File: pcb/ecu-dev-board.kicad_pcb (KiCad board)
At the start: 4 copper layers, 99.9 x 99.9 mm, 218 parts, among them IC1 MAX9924UAUB+, IC2 74HC14D-Q100,118, IC3 UCC28910DR, IC4 UCC27624QDRQ1, J1 MX23A18NF1, J2 39-30-1020, K1 Relay, Q1 MMBT2222A, Q10 AO3400A, Q2 IRLIZ44N, Q3 HL2303, Q4 STGB20M65DF2, Q5 MMBT2222A, Q6 MMBT2222A, Q7 MMBT2222A, Q8 MMBTA55, Q9 MMBTA55, T1 SM-LP-5001E, U1 WeMos_S2_mini, U2 OPA2376xxD, U3 TPS54202DDC, U4 AT223-CuH-S

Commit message: organized pcb
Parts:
- moved JP10 142.6 mm to (134.5, 188.7)
- moved TP24 135.6 mm to (39.1, 151.6)
- moved TP25 135.6 mm to (39.1, 154.7)
- moved TP26 135.6 mm to (39.1, 157.7)
- moved JP4 131.7 mm to (139.3, 185.5)
- moved JP7 131.7 mm to (139.3, 192.6)
- moved JP5 131.7 mm to (139.3, 189.0)
- moved TP30 120.9 mm to (43.8, 152.1)
- moved TP31 120.9 mm to (43.7, 159.6)
- moved TP10 111.3 mm to (34.9, 154.4)
- moved TP11 111.3 mm to (34.9, 157.4)
- moved TP19 111.3 mm to (34.9, 160.5)
- moved TP9 111.3 mm to (34.9, 151.3)
- moved JP8 98.2 mm to (134.4, 178.5)
- moved JP25 98.2 mm to (134.4, 185.6)
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
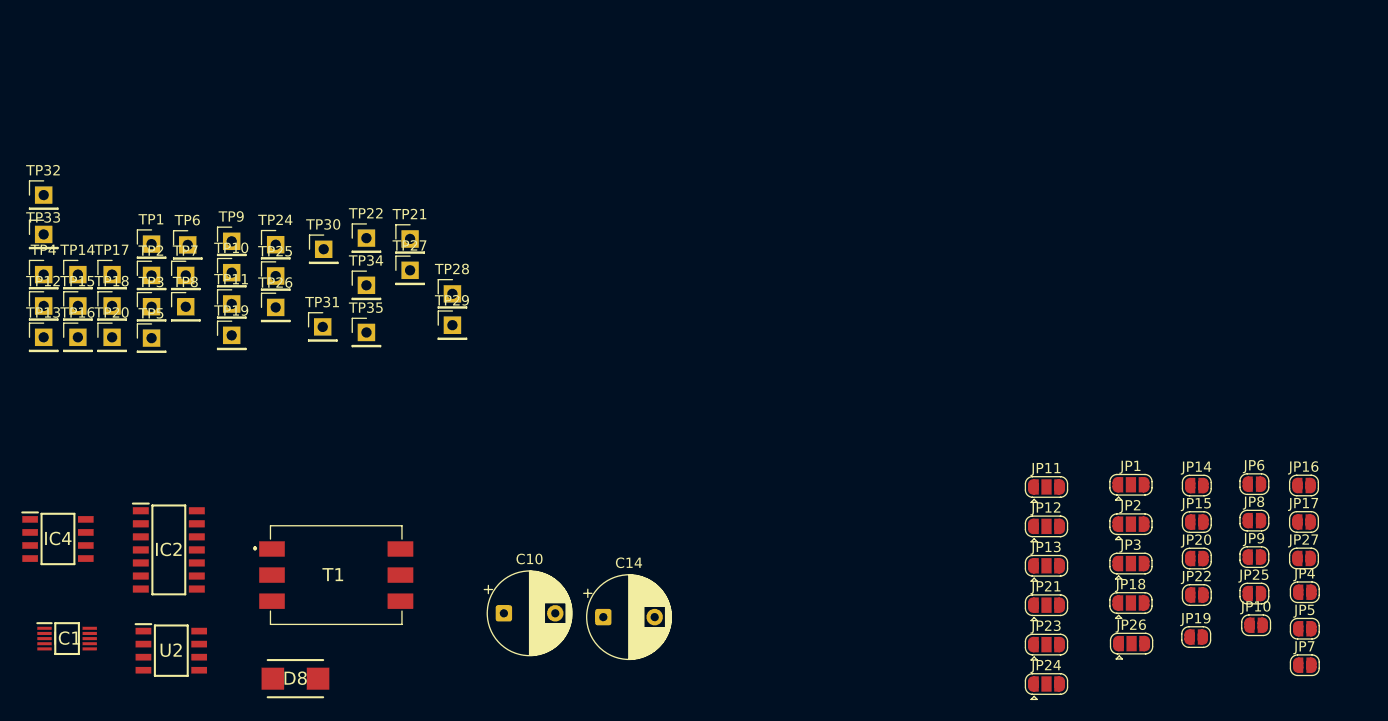
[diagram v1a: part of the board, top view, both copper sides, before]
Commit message: ordered jumpers and test pins
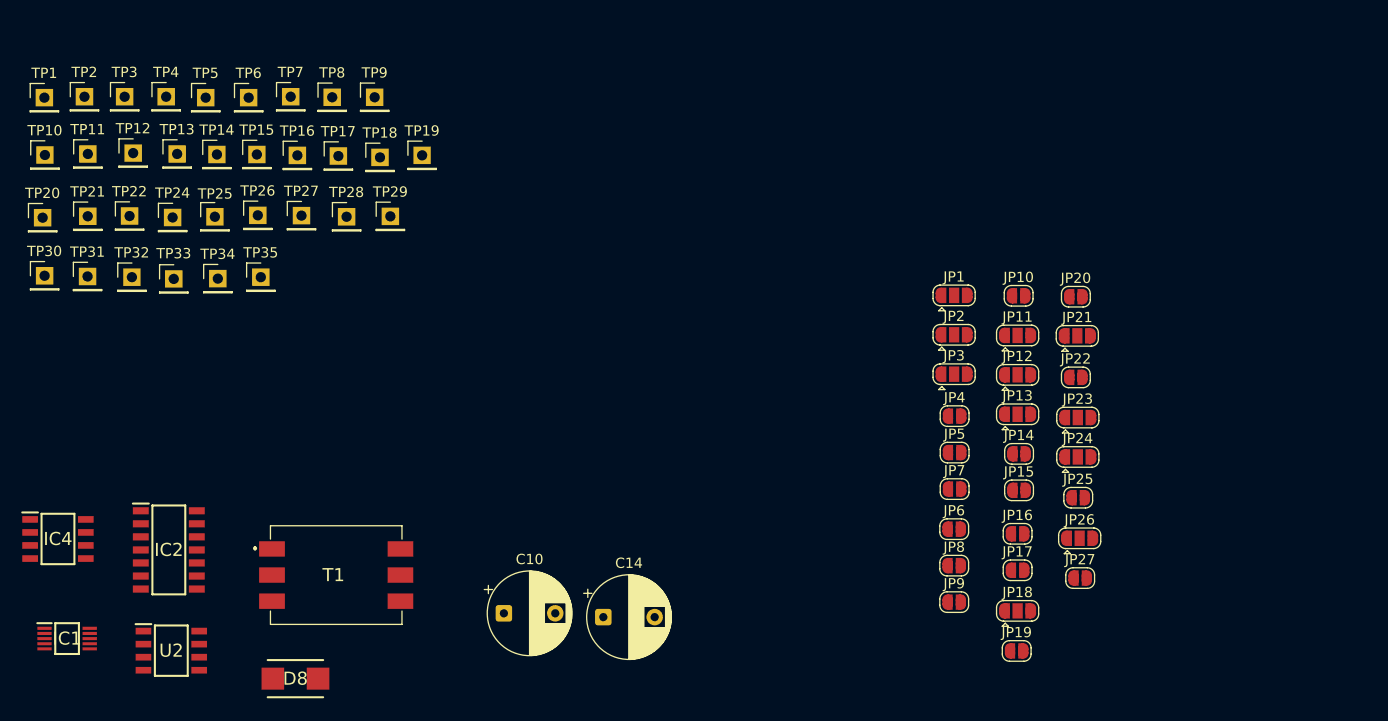
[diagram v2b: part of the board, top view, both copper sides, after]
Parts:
- moved JP10 39.5 mm to (111.4, 156.6)
- moved JP4 38.1 mm to (105.2, 168.3)
- moved JP7 38.1 mm to (105.2, 175.4)
- moved JP5 38.1 mm to (105.2, 171.9)
- moved TP21 31.4 mm to (20.8, 148.9)
- moved TP18 29.8 mm to (49.3, 143.1)
- moved JP6 29.5 mm to (105.2, 179.3)
- moved JP8 29.5 mm to (105.2, 182.9)
- moved JP9 29.5 mm to (105.2, 186.4)
- moved JP16 28.3 mm to (111.3, 179.8)
- moved JP17 28.3 mm to (111.3, 183.3)
- moved JP20 28.1 mm to (117.0, 156.7)
- moved TP16 27.7 mm to (41.2, 142.9)
- moved TP30 27.3 mm to (16.6, 154.7)
- moved JP21 26.4 mm to (117.1, 160.5)
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
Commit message: revision 2.0: added LC Vbatt filtering and changed Pmos protection to be a schttoky
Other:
- board text added: "1 Layer: piste corte (alimentazione solo piste cortissime con via dal layer 4) 2 Layer: tutta massa ininterrotta 3 Layer: segnali 4 Layer: alimentazione"
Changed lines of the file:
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@@
 		(layer "Edge.Cuts")
+	)
+	(gr_text "1 Layer: piste corte (alimentazione solo piste cortissime con via dal layer 4)\n2 Layer: tutta massa ininterrotta\n3 Layer: segnali\n4 Layer: alimentazione"
+		(at 197.92 9.56 0)
+		(layer "Cmts.User")
+		(effects
+			(font
+				(size 1.5 1.5)
+				(thickness 0.3)
+				(bold yes)
+			)
+			(justify left bottom)
+		)
 	)
 	(gr_text "TROPPO GRANDI"

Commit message: revision 2.0: other minor changed
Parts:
- removed BR2: MB10S, SamacSys_Parts:SOP245P670X290-4N
- removed C20: 10u, Capacitor_SMD:C_0603_1608Metric
- removed FB1, FB2: BLM18PG121SN1D, SamacSys_Parts:BLM18SP221SN1B
- removed JP20, JP6: SolderJumper_2_Open, Jumper:SolderJumper-2_P1.3mm_Open_RoundedPad1.0x1.5mm
- removed Q3: HL2303, Package_TO_SOT_SMD:SOT-23
- removed R16: 510k, Resistor_SMD:R_0603_1608Metric
- removed R17: 100k, Resistor_SMD:R_0603_1608Metric
- removed R36: 5k1, Resistor_SMD:R_0603_1608Metric
- added C603: 22u, Capacitor_SMD:C_0805_2012Metric, F.Cu at (110.8, 123.0)
- added C612: 1000u, Capacitor_THT:CP_Radial_D8.0mm_P5.00mm, F.Cu at (66.1, 91.4)
- added C613: 10u, Capacitor_SMD:C_0805_2012Metric, F.Cu at (110.8, 126.1)
- added C614: 1u, Capacitor_SMD:C_0805_2012Metric, F.Cu at (110.8, 129.1)
- added C615: 100n, Capacitor_SMD:C_0805_2012Metric, F.Cu at (110.8, 132.1)
- added D609: SS54, Diode_SMD:D_SMA, F.Cu at (117.1, 123.8)
- added FB601: BLM18PG121SN1D, Inductor_SMD:L_0603_1608Metric, F.Cu at (115.0, 127.3)
- added H601: MountingHole_Pad, MountingHole:MountingHole_3.2mm_M3_DIN965_Pad, F.Cu at (105.0, 113.2)
- added H602: MountingHole_Pad, MountingHole:MountingHole_3.2mm_M3_DIN965_Pad, F.Cu at (105.0, 120.3)
- added H603: MountingHole_Pad, MountingHole:MountingHole_3.2mm_M3_DIN965_Pad, F.Cu at (105.0, 127.5)
- added H604: MountingHole_Pad, MountingHole:MountingHole_3.2mm_M3_DIN965_Pad, F.Cu at (248.9, 116.8)
- added L603: 15u, Inductor_SMD:L_10.4x10.4_H4.8, F.Cu at (114.9, 115.6)
- C201: renamed from C5; footprint Capacitor_SMD:C_0603_1608Metric -> Capacitor_SMD:C_0805_2012Metric
- C202: renamed from C6; footprint Capacitor_SMD:C_0603_1608Metric -> Capacitor_SMD:C_0805_2012Metric
- C203: renamed from C1; footprint Capacitor_SMD:C_0603_1608Metric -> Capacitor_SMD:C_0805_2012Metric
- C204: renamed from C29; footprint Capacitor_SMD:C_0603_1608Metric -> Capacitor_SMD:C_0805_2012Metric
- C205: renamed from C28; footprint Capacitor_SMD:C_0603_1608Metric -> Capacitor_SMD:C_0805_2012Metric
- C206: renamed from C7; footprint Capacitor_SMD:C_0603_1608Metric -> Capacitor_SMD:C_0805_2012Metric
- C207: renamed from C8; footprint Capacitor_SMD:C_0603_1608Metric -> Capacitor_SMD:C_0805_2012Metric
- C208: renamed from C2; footprint Capacitor_SMD:C_0603_1608Metric -> Capacitor_SMD:C_0805_2012Metric
- C209: renamed from C3; footprint Capacitor_SMD:C_0603_1608Metric -> Capacitor_SMD:C_0805_2012Metric
- C210: renamed from C4; footprint Capacitor_SMD:C_0603_1608Metric -> Capacitor_SMD:C_0805_2012Metric
- C401: renamed from C15; footprint Capacitor_SMD:C_0603_1608Metric -> Capacitor_SMD:C_0805_2012Metric
- C402: renamed from C35; footprint Capacitor_SMD:C_0603_1608Metric -> Capacitor_SMD:C_0805_2012Metric
- C403: renamed from C18; footprint Capacitor_SMD:C_0603_1608Metric -> Capacitor_SMD:C_0805_2012Metric
- C404: renamed from C16; footprint Capacitor_SMD:C_0603_1608Metric -> Capacitor_SMD:C_0805_2012Metric
- C405: renamed from C32; footprint Capacitor_SMD:C_0603_1608Metric -> Capacitor_SMD:C_0805_2012Metric
- C406: renamed from C33; footprint Capacitor_SMD:C_0603_1608Metric -> Capacitor_SMD:C_0805_2012Metric
- C407: renamed from C34; footprint Capacitor_SMD:C_0603_1608Metric -> Capacitor_SMD:C_0805_2012Metric
- C408: renamed from C27; footprint Capacitor_SMD:C_0603_1608Metric -> Capacitor_SMD:C_0805_2012Metric
- C409: renamed from C11; footprint Capacitor_SMD:C_0603_1608Metric -> Capacitor_SMD:C_0805_2012Metric
- C410: renamed from C30; footprint Capacitor_SMD:C_0603_1608Metric -> Capacitor_SMD:C_0805_2012Metric
- C411: renamed from C31; footprint Capacitor_SMD:C_0603_1608Metric -> Capacitor_SMD:C_0805_2012Metric
- C604: renamed from C21; footprint Capacitor_SMD:C_0603_1608Metric -> Capacitor_SMD:C_0805_2012Metric
- C605: renamed from C22; footprint Capacitor_SMD:C_0603_1608Metric -> Capacitor_SMD:C_0805_2012Metric
- C606: renamed from C23; footprint Capacitor_SMD:C_0603_1608Metric -> Capacitor_SMD:C_0805_2012Metric
- C608: renamed from C24; footprint Capacitor_SMD:C_0603_1608Metric -> Capacitor_SMD:C_0805_2012Metric
- C609: renamed from C17; footprint Capacitor_SMD:C_0603_1608Metric -> Capacitor_SMD:C_0805_2012Metric
- C610: renamed from C25; footprint Capacitor_SMD:C_0603_1608Metric -> Capacitor_SMD:C_0805_2012Metric
- C611: renamed from C13; footprint Capacitor_SMD:C_0603_1608Metric -> Capacitor_SMD:C_0805_2012Metric
- C616: renamed from C19; value 1m -> 1000u
- C701: renamed from C37; footprint Capacitor_SMD:C_0603_1608Metric -> Capacitor_SMD:C_0805_2012Metric
- C702: renamed from C36; footprint Capacitor_SMD:C_0603_1608Metric -> Capacitor_SMD:C_0805_2012Metric
- C703: renamed from C26; footprint Capacitor_SMD:C_0603_1608Metric -> Capacitor_SMD:C_0805_2012Metric
- IC701: renamed from IC4; value UCC27624QDRQ1 -> UCC27624DR
- L601: renamed from L3; footprint Inductor_SMD:L_SXN_SMDRI125 -> Inductor_SMD:L_10.4x10.4_H4.8
- R201: renamed from R6; footprint Resistor_SMD:R_0603_1608Metric -> Resistor_SMD:R_0805_2012Metric
- R202: renamed from R7; footprint Resistor_SMD:R_0603_1608Metric -> Resistor_SMD:R_0805_2012Metric
- R203: renamed from R4; footprint Resistor_SMD:R_0603_1608Metric -> Resistor_SMD:R_0805_2012Metric
- R204: renamed from R5; footprint Resistor_SMD:R_0603_1608Metric -> Resistor_SMD:R_0805_2012Metric
- R205: renamed from R1; footprint Resistor_SMD:R_0603_1608Metric -> Resistor_SMD:R_0805_2012Metric
- R206: renamed from R2; footprint Resistor_SMD:R_0603_1608Metric -> Resistor_SMD:R_0805_2012Metric
- R207: renamed from R55; footprint Resistor_SMD:R_0603_1608Metric -> Resistor_SMD:R_0805_2012Metric
- R208: renamed from R3; footprint Resistor_SMD:R_0603_1608Metric -> Resistor_SMD:R_0805_2012Metric
- R209: renamed from R8; footprint Resistor_SMD:R_0603_1608Metric -> Resistor_SMD:R_0805_2012Metric
- R210: renamed from R10; footprint Resistor_SMD:R_0603_1608Metric -> Resistor_SMD:R_0805_2012Metric
- R211: renamed from R11; footprint Resistor_SMD:R_0603_1608Metric -> Resistor_SMD:R_0805_2012Metric
- R213: renamed from R12; footprint Resistor_SMD:R_0603_1608Metric -> Resistor_SMD:R_0805_2012Metric
- R214: renamed from R57; footprint Resistor_SMD:R_0603_1608Metric -> Resistor_SMD:R_0805_2012Metric
- R301: renamed from R50; footprint Resistor_SMD:R_0603_1608Metric -> Resistor_SMD:R_0805_2012Metric
- R302: renamed from R51; footprint Resistor_SMD:R_0603_1608Metric -> Resistor_SMD:R_0805_2012Metric
- R303: renamed from R52; footprint Resistor_SMD:R_0603_1608Metric -> Resistor_SMD:R_0805_2012Metric
- R401: renamed from R29; footprint Resistor_SMD:R_0603_1608Metric -> Resistor_SMD:R_0805_2012Metric
- R402: renamed from R30; footprint Resistor_SMD:R_0603_1608Metric -> Resistor_SMD:R_0805_2012Metric
- R403: renamed from R62; footprint Resistor_SMD:R_0603_1608Metric -> Resistor_SMD:R_0805_2012Metric
- R404: renamed from R63; footprint Resistor_SMD:R_0603_1608Metric -> Resistor_SMD:R_0805_2012Metric
- R405: renamed from R28; footprint Resistor_SMD:R_0603_1608Metric -> Resistor_SMD:R_0805_2012Metric
- R406: renamed from R25; footprint Resistor_SMD:R_0603_1608Metric -> Resistor_SMD:R_0805_2012Metric
- R407: renamed from R32; footprint Resistor_SMD:R_0603_1608Metric -> Resistor_SMD:R_0805_2012Metric
- R408: renamed from R31; footprint Resistor_SMD:R_0603_1608Metric -> Resistor_SMD:R_0805_2012Metric
- R409: renamed from R64; footprint Resistor_SMD:R_0603_1608Metric -> Resistor_SMD:R_0805_2012Metric
- R410: renamed from R59; footprint Resistor_SMD:R_0603_1608Metric -> Resistor_SMD:R_0805_2012Metric
- R411: renamed from R60; footprint Resistor_SMD:R_0603_1608Metric -> Resistor_SMD:R_0805_2012Metric
- R412: renamed from R61; footprint Resistor_SMD:R_0603_1608Metric -> Resistor_SMD:R_0805_2012Metric
- R413: renamed from R19; footprint Resistor_SMD:R_0603_1608Metric -> Resistor_SMD:R_0805_2012Metric
- R414: renamed from R53; footprint Resistor_SMD:R_0603_1608Metric -> Resistor_SMD:R_0805_2012Metric
- R415: renamed from R54; footprint Resistor_SMD:R_0603_1608Metric -> Resistor_SMD:R_0805_2012Metric
- R416: renamed from R47; footprint Resistor_SMD:R_0603_1608Metric -> Resistor_SMD:R_0805_2012Metric
- R417: renamed from R58; footprint Resistor_SMD:R_0603_1608Metric -> Resistor_SMD:R_0805_2012Metric
- R418: renamed from R20; footprint Resistor_SMD:R_0603_1608Metric -> Resistor_SMD:R_0805_2012Metric
- R419: renamed from R37; footprint Resistor_SMD:R_0603_1608Metric -> Resistor_SMD:R_0805_2012Metric
- R420: renamed from R22; footprint Resistor_SMD:R_0603_1608Metric -> Resistor_SMD:R_0805_2012Metric
- R421: renamed from R21; footprint Resistor_SMD:R_0603_1608Metric -> Resistor_SMD:R_0805_2012Metric
- R501: renamed from R48; footprint Resistor_SMD:R_0603_1608Metric -> Resistor_SMD:R_0805_2012Metric
- R502: renamed from R68; footprint Resistor_SMD:R_0603_1608Metric -> Resistor_SMD:R_0805_2012Metric
- R503: renamed from R49; footprint Resistor_SMD:R_0603_1608Metric -> Resistor_SMD:R_0805_2012Metric
- R504: renamed from R56; footprint Resistor_SMD:R_0603_1608Metric -> Resistor_SMD:R_0805_2012Metric
- R505: renamed from R15; footprint Resistor_SMD:R_0603_1608Metric -> Resistor_SMD:R_0805_2012Metric
- R506: renamed from R45; footprint Resistor_SMD:R_0603_1608Metric -> Resistor_SMD:R_0805_2012Metric
- R507: renamed from R13; footprint Resistor_SMD:R_0603_1608Metric -> Resistor_SMD:R_0805_2012Metric
- R508: renamed from R46; footprint Resistor_SMD:R_0603_1608Metric -> Resistor_SMD:R_0805_2012Metric
- R509: renamed from R67; footprint Resistor_SMD:R_0603_1608Metric -> Resistor_SMD:R_0805_2012Metric
- R510: renamed from R18; value 330k -> 1M; footprint Resistor_SMD:R_0603_1608Metric -> Resistor_SMD:R_0805_2012Metric
- R602: renamed from R34; footprint Resistor_SMD:R_0603_1608Metric -> Resistor_SMD:R_0805_2012Metric
- R603: renamed from R9; footprint Resistor_SMD:R_0603_1608Metric -> Resistor_SMD:R_0805_2012Metric
- R604: renamed from R33; footprint Resistor_SMD:R_0603_1608Metric -> Resistor_SMD:R_0805_2012Metric
- R605: renamed from R24; footprint Resistor_SMD:R_0603_1608Metric -> Resistor_SMD:R_0805_2012Metric
- R606: renamed from R23; footprint Resistor_SMD:R_0603_1608Metric -> Resistor_SMD:R_0805_2012Metric
- R607: renamed from R26; footprint Resistor_SMD:R_0603_1608Metric -> Resistor_SMD:R_0805_2012Metric
- R608: renamed from R35; footprint Resistor_SMD:R_0603_1608Metric -> Resistor_SMD:R_0805_2012Metric
- R609: renamed from R44; footprint Resistor_SMD:R_0603_1608Metric -> Resistor_SMD:R_0805_2012Metric
- R610: renamed from R43; footprint Resistor_SMD:R_0603_1608Metric -> Resistor_SMD:R_0805_2012Metric
- R611: renamed from R65; footprint Resistor_SMD:R_0603_1608Metric -> Resistor_SMD:R_0805_2012Metric
- R702: renamed from R14; footprint Resistor_SMD:R_0603_1608Metric -> Resistor_SMD:R_0805_2012Metric
- R703: renamed from R38; footprint Resistor_SMD:R_0603_1608Metric -> Resistor_SMD:R_0805_2012Metric
- R704: renamed from R39; footprint Resistor_SMD:R_0603_1608Metric -> Resistor_SMD:R_0805_2012Metric
- R706: renamed from R40; footprint Resistor_SMD:R_0603_1608Metric -> Resistor_SMD:R_0805_2012Metric
- moved J102 82.4 mm to (162.6, 130.0)
- moved D301 49.4 mm to (168.7, 124.0)
- moved J101 21.8 mm to (202.9, 125.1)
- moved R301 5.68 mm to (112.0, 18.9)
- moved R303 5.68 mm to (112.0, 23.9)
- moved R302 5.68 mm to (112.0, 21.4)
- renumbered C9 to C501, C10 to C601, C12 to C602, C14 to C607, D15 to D201, D14 to D301, D11 to D401, D18 to D402, D22 to D403, D17 to D404, D16 to D405, D13 to D501, D12 to D502, D4 to D503, D2 to D504, D3 to D505, D5 to D506, D8 to D601, D7 to D602, D21 to D603, D10 to D604, D9 to D605, D23 to D606, D1 to D607, D19 to D608, D6 to D610, D20 to D611, IC1 to IC201, IC2 to IC401, IC3 to IC601, J1 to J101, J2 to J102, JP19 to JP201, JP3 to JP202, JP1 to JP203, JP18 to JP204, JP2 to JP205, JP16 to JP206, JP17 to JP207, JP27 to JP208, JP12 to JP401, JP11 to JP402, JP14 to JP403, JP15 to JP404, JP13 to JP405, JP21 to JP406, JP24 to JP407, JP23 to JP408, JP22 to JP410, JP4 to JP501, JP7 to JP502, JP5 to JP503, JP8 to JP601, JP26 to JP602, JP25 to JP603, JP9 to JP604, JP10 to JP605, K1 to K501, L1 to L602, Q7 to Q201, Q6 to Q501, Q8 to Q502, Q1 to Q503, Q9 to Q504, Q5 to Q505, Q2 to Q701, Q4 to Q702, Q10 to Q703, R66 to R212, R27 to R601, R42 to R701, R41 to R705, T1 to T201, TP1 to TP201, TP2 to TP202, TP5 to TP203, TP6 to TP204, TP3 to TP205, TP8 to TP206, TP7 to TP207, TP35 to TP301, TP34 to TP302, TP22 to TP303, TP25 to TP304, TP26 to TP305, TP24 to TP306, TP15 to TP401, TP16 to TP402, TP17 to TP403, TP4 to TP404, TP20 to TP405, TP14 to TP406, TP13 to TP407, TP12 to TP408, TP32 to TP409, TP33 to TP410, TP18 to TP411, TP30 to TP501, TP9 to TP502, TP19 to TP503, TP10 to TP504, TP31 to TP505, TP11 to TP506, TP28 to TP601, TP29 to TP602, TP27 to TP701, TP21 to TP702, U4 to U201, U1 to U301, U2 to U401, U3 to U601, Z2 to Z201, Z1 to Z701
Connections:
- C408 pad 2: Net-(D22-K) -> Net-(D403-K)
- D403 pad 1: Net-(D22-K) -> Net-(D403-K)
- D403 pad 2: Net-(D22-A) -> DIGITAL_QS_IN
- D602 pad 1: Net-(D7-K) -> /PSU/RECT+
- D602 pad 2: Net-(BR2-~{_1}) -> Net-(D602-A)
- IC401 pad 3: DIGITAL_QS_IN -> Net-(D403-K)
- J101 pad 3: +12V -> +BATT
- JP601 pad 2: Net-(D7-K) -> Net-(D602-A)
- JP602 pad 2: Net-(BR2-~{_2}) -> /PSU/RECT-
- R414 pad 1: Net-(D22-A) -> DIGITAL_QS_IN
- R415 pad 1: Net-(D22-K) -> Net-(D403-K)
- R415 pad 2: Net-(D22-A) -> DIGITAL_QS_IN
- U601 pad 5: Net-(U3-EN) -> unconnected-(U601-EN-Pad5)
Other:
- board text added: "ANALOG"
- board text added: "DIGITAL"
- board text added: "POWER"

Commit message: pcb first iteration of power implementation
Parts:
- C601, C607: footprint Capacitor_THT:CP_Radial_D8.0mm_P5.00mm -> Capacitor_THT:CP_Radial_D5.0mm_P2.50mm
- JP201, JP202, JP203, JP204, JP205, JP206, JP207, JP208, JP401, JP402, JP403, JP404, JP405, JP406, JP407, JP408, JP410, JP501, JP502, JP503, JP601, JP602, JP603, JP604, JP605: moved to B.Cu
- moved IC701 229.0 mm to (224.0, 80.4), turned to -90 degrees
- moved U401 205.5 mm to (176.7, 48.3)
- moved D603 196.0 mm to (228.7, 98.8), turned to 180 degrees
- moved C601 188.0 mm to (235.9, 117.8)
- moved IC201 184.1 mm to (176.4, 94.7), turned to 90 degrees
- moved IC401 183.2 mm to (176.5, 73.1)
- moved T201 173.3 mm to (188.8, 87.4), turned to -90 degrees
- moved D606 169.1 mm to (201.2, 108.4)
- moved C605 166.0 mm to (237.2, 108.9), turned to 180 degrees
- moved C612 165.9 mm to (229.2, 121.8), turned to 90 degrees
- moved Q701 165.6 mm to (209.1, 93.0)
- moved C604 162.2 mm to (231.5, 111.8), turned to 90 degrees
- moved D601 158.4 mm to (182.1, 121.8)
- moved C608 155.0 mm to (227.5, 107.6)
- moved C606 154.8 mm to (227.6, 104.1)
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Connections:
- C601 pad 1: /PSU/FB_12 -> +12V
- C603 pad 1: /PSU/FB_12 -> +12V
- C604 pad 1: /PSU/FB_12 -> +12V
- U601 pad 3: /PSU/FB_12 -> +12V
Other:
- board text removed: "TROPPO GRANDI"

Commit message: moved ac-dc converter
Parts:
- moved TP602 165.3 mm to (207.8, 98.8)
- moved TP601 164.9 mm to (203.1, 98.8)
- moved JP602 18.5 mm to (198.4, 121.3), turned to 90 degrees
- moved JP601 18.3 mm to (194.7, 122.2)
- moved D602 12.6 mm to (191.3, 122.2), turned to 0 degrees
- moved C616 7.19 mm to (197.0, 92.2)
- moved R601 5.34 mm to (186.9, 115.8), turned to -90 degrees
- moved C602 4.90 mm to (179.6, 112.7)
- moved D605 4.54 mm to (193.0, 117.4)
- moved D606 4.50 mm to (201.3, 103.9)
- moved D607 4.50 mm to (197.3, 100.2)
- moved FB601 4.50 mm to (170.8, 95.1)
- moved IC401 4.50 mm to (176.6, 68.6)
- moved IC601 4.50 mm to (191.8, 111.7)
- moved L602 4.50 mm to (203.3, 112.5)
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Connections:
- J101 pad 6: STATOR -> STATOR_2
- J101 pad 7: STATOR_2 -> STATOR
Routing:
- net /PSU/RECT+: track 0.00 -> 14.8 mm
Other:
- board text added: "+ 5V -"

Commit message: placed CDI components
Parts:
- moved TP501 234.3 mm to (239.5, 82.3)
- moved C501 231.6 mm to (248.7, 90.8), turned to -90 degrees
- moved R507 224.2 mm to (235.5, 88.2)
- moved D505 220.9 mm to (249.5, 130.0), turned to -90 degrees
- moved R502 216.3 mm to (239.4, 79.2)
- moved R506 215.3 mm to (227.2, 87.3), turned to -90 degrees
- moved Q501 214.0 mm to (239.4, 74.8), turned to 90 degrees
- moved Q502 212.7 mm to (239.5, 70.5), turned to 90 degrees
- moved Q503 212.5 mm to (231.6, 91.2), turned to 90 degrees
- moved D504 210.7 mm to (239.2, 99.6), turned to -90 degrees
- moved D501 207.7 mm to (247.1, 82.8), turned to -90 degrees
- moved D503 207.1 mm to (241.8, 119.2), turned to -90 degrees
- moved Q504 207.1 mm to (231.8, 87.2), turned to 90 degrees
- moved TP503 194.2 mm to (239.5, 87.4)
- moved R603 188.6 mm to (259.8, 117.3)
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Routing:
- net /PSU/RECT+: track 14.8 -> 28.1 mm

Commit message: started analogue and signal digital part
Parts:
- removed TP206, TP207: TestPoint, Connector_PinHeader_2.54mm:PinHeader_1x01_P2.54mm_Vertical
- moved TP506 223.9 mm to (243.8, 121.9)
- moved TP504 220.8 mm to (231.4, 91.6)
- moved TP505 211.2 mm to (219.7, 83.7)
- moved D506 209.8 mm to (250.4, 110.1), turned to 90 degrees
- moved Q505 195.4 mm to (214.6, 93.0)
- moved D201 192.0 mm to (211.0, 74.3)
- moved R509 189.7 mm to (211.6, 93.0), turned to -90 degrees
- moved R214 181.2 mm to (204.6, 78.6), turned to 90 degrees
- moved Z201 178.5 mm to (211.0, 76.8)
- moved D502 172.7 mm to (219.7, 89.2), turned to 90 degrees
- moved R510 170.5 mm to (230.3, 79.6)
- moved H603 168.4 mm to (248.9, 39.9)
- moved JP501 160.0 mm to (248.7, 76.8), turned to -90 degrees
- moved K501 157.5 mm to (223.3, 91.3)
- moved R508 150.9 mm to (207.3, 92.0)
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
